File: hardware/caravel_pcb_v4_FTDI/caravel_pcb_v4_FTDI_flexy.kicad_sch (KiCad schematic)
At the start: 65 parts, among them J1 USB_B_Micro - 10118193-0001LF, J10 Conn_01x27_Female, J11 Conn_01x20_Female, J2 Conn_01x02_Female, J3 Conn_01x02_Male, J4 Conn_01x04_Female, J5 Conn_01x02_Male, J6 Conn_01x02_Male, J7 Conn_01x06_Female, J8 Conn_01x02_Male, J9 Conn_01x02_Male, SW1 SW_Push - SKQGADE010, T1 Logo, T2 Logo, U1 FT232H, U2 SN74LVC1G125DCKR, U3 SN74LVC1G125DCKR, U4 AZ1117CH-1.8TRG1, U5 AZ1117-3.3, U6 caravel_breakout, U7 W25Q32FVSS, X1 DSC6001_10MHZ, Y1 CSTNE12M0GH5L000R0

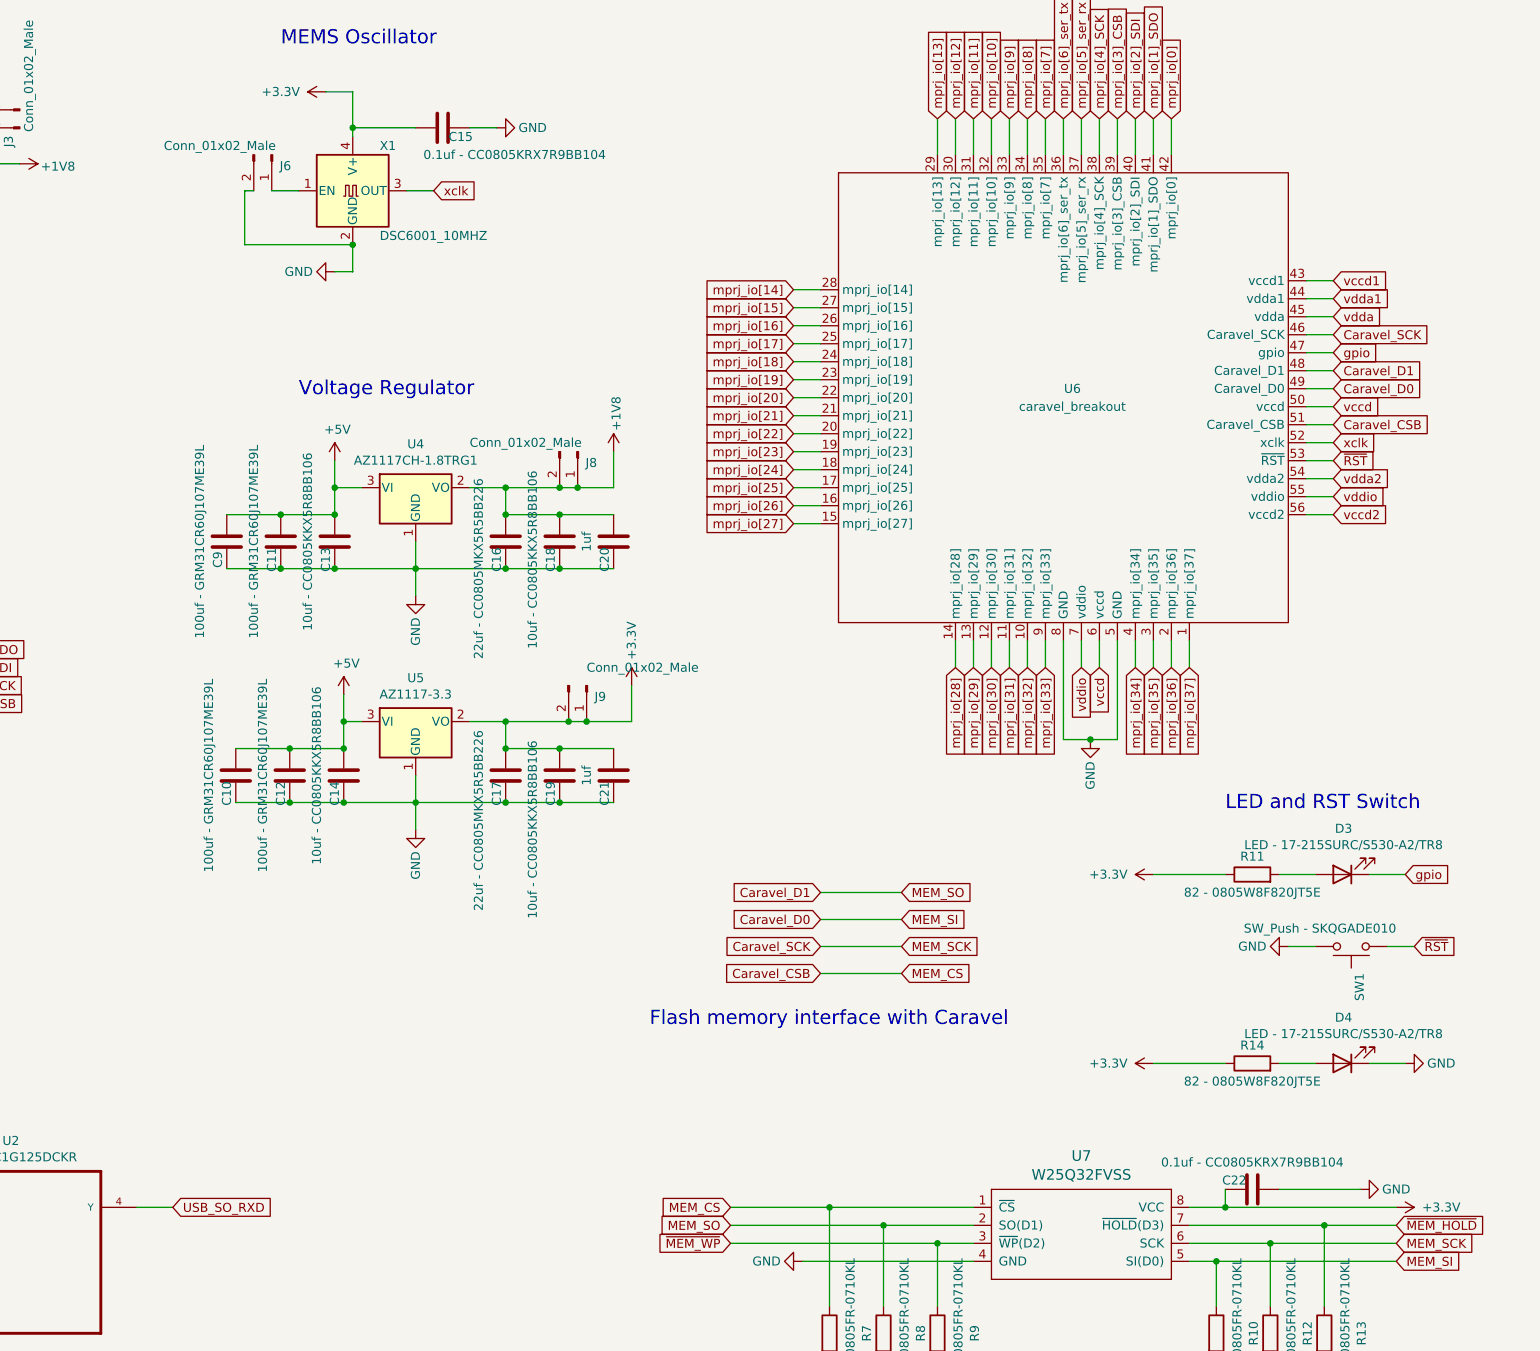
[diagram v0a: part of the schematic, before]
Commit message: update caravel FTDI mainboard V4 (Rev 4B)
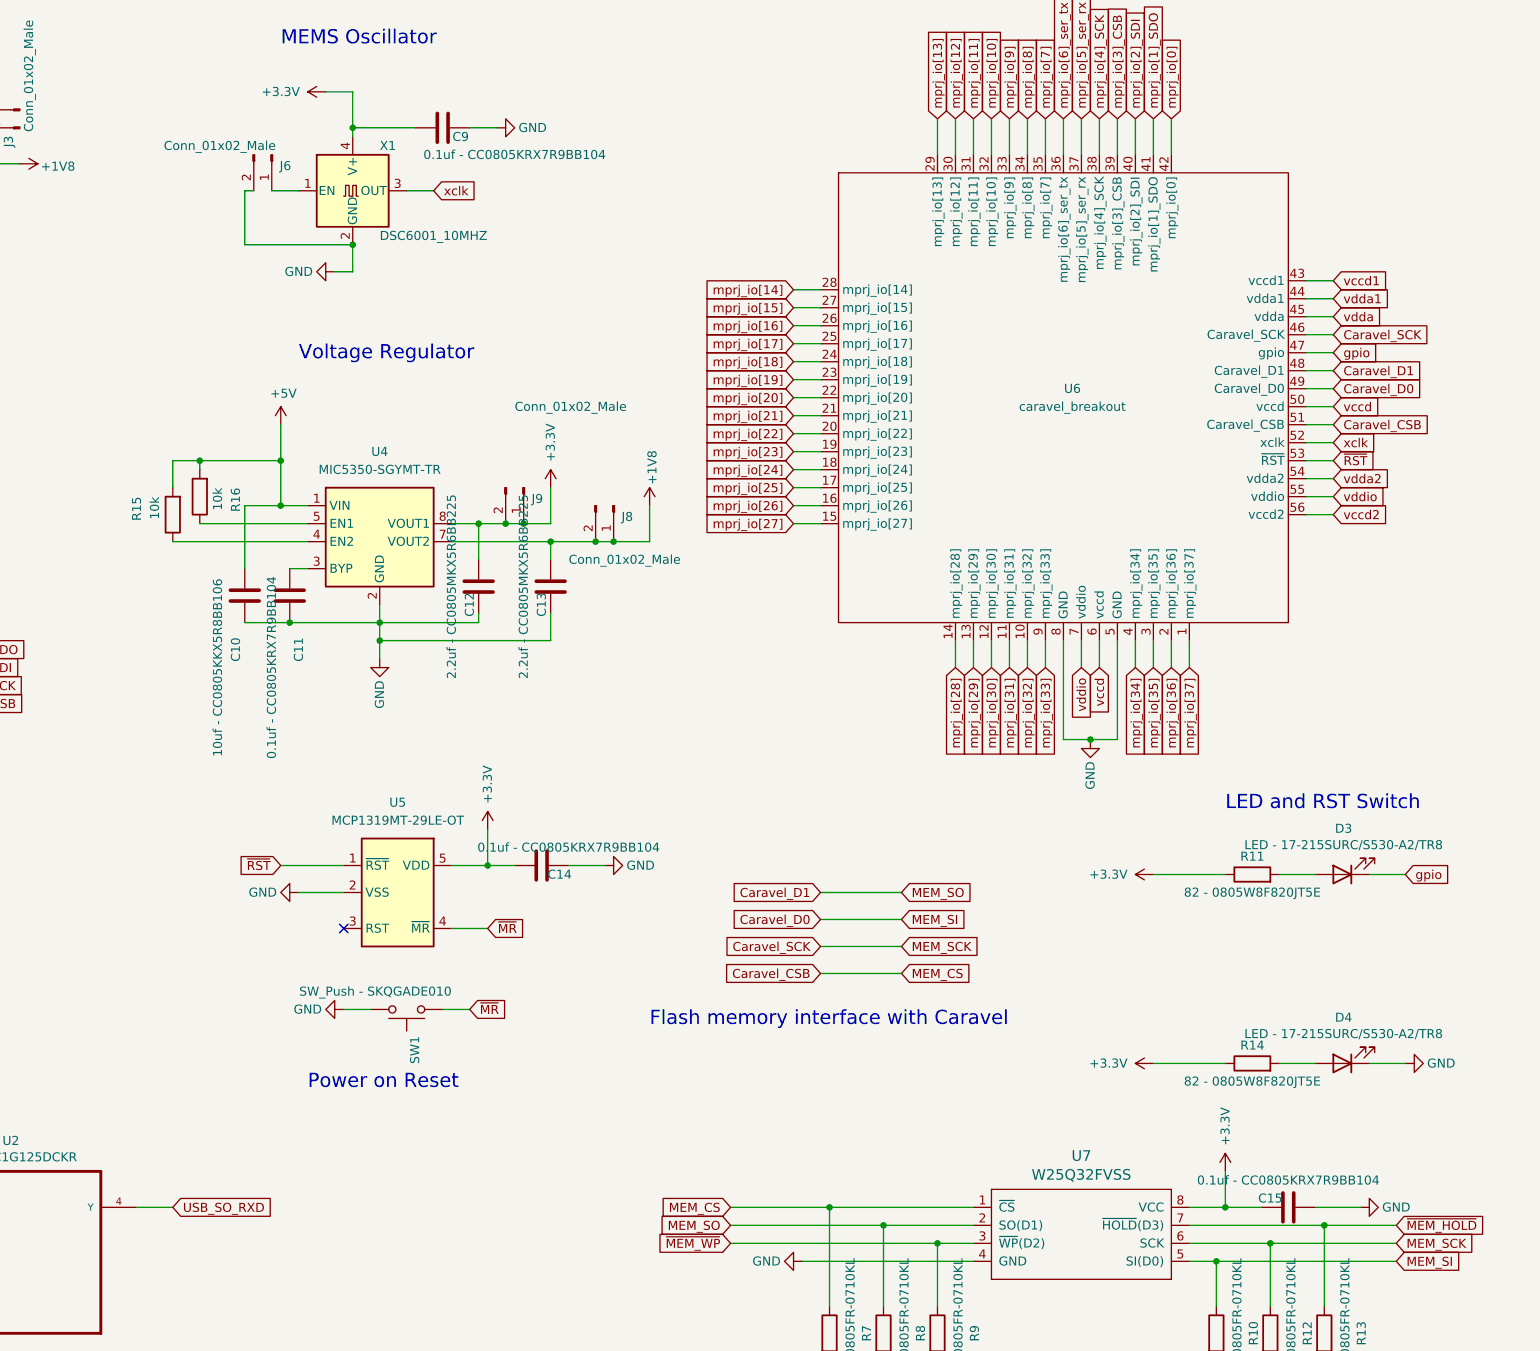
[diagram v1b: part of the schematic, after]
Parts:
- removed C16, C17: 22uf - CC0805MKX5R5BB226, Capacitor_SMD:C_0805_2012Metric, symbol Device:C
- removed C18, C19: 10uf - CC0805KKX5R8BB106, Capacitor_SMD:C_0805_2012Metric, symbol Device:C
- removed C20, C21: 1uf, Capacitor_SMD:C_0805_2012Metric, symbol Device:C
- removed C9: 100uf - GRM31CR60J107ME39L, Capacitor_SMD:C_1206_3216Metric, symbol Device:C
- removed U4: AZ1117CH-1.8TRG1, Package_TO_SOT_SMD:SOT-223, symbol Regulator_Linear:AZ1117-1.8
- removed U5: AZ1117-3.3, Package_TO_SOT_SMD:SOT-223, symbol Regulator_Linear:AZ1117-3.3
- added R15, R16: 10k, Resistor_SMD:R_0805_2012Metric, symbol Device:R
- added U4: MIC5350-SGYMT-TR, Package_DFN_QFN:DFN-8-1EP_2x2mm_P0.5mm_EP0.6x1.2mm, symbol Caravel_board:MIC5350-SGYMT-TR
- added U5: MCP1319MT-29LE-OT, Caravel_Board:PoR_5_SOT23, symbol Caravel_board:MCP1319MT-29LE-OT
- C10: value 100uf - GRM31CR60J107ME39L -> 10uf - CC0805KKX5R8BB106; footprint Capacitor_SMD:C_1206_3216Metric -> Capacitor_SMD:C_0805_2012Metric
- C11: value 100uf - GRM31CR60J107ME39L -> 0.1uf - CC0805KRX7R9BB104; footprint Capacitor_SMD:C_1206_3216Metric -> Capacitor_SMD:C_0805_2012Metric
- C12: value 100uf - GRM31CR60J107ME39L -> 2.2uf - CC0805MKX5R6BB225; footprint Capacitor_SMD:C_1206_3216Metric -> Capacitor_SMD:C_0805_2012Metric
- C13: value 10uf - CC0805KKX5R8BB106 -> 2.2uf - CC0805MKX5R6BB225
- C14: value 10uf - CC0805KKX5R8BB106 -> 0.1uf - CC0805KRX7R9BB104
- renumbered C22 to C15, C15 to C9
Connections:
- net +1V8: now also C13.2, U4.7 (VOUT2)
- net +3V3: now also C12.2, C14.2, U4.8 (VOUT1), U5.5 (VDD)
- net +5V: now also R15.2, R16.2, U4.1 (VIN); no longer C11.2, C12.2, C13.2, C14.2
- net GND: now also C11.2, U4.2 (GND), U4.9 (GND), U5.2 (VSS); no longer C11.1
- net ~{RST}: now also U5.1 (~{RST}); no longer SW1.1
- new net: R16.1, U4.5 (EN1)
- new net: R15.1, U4.4 (EN2)
- new net: C11.1, U4.3 (BYP)
- new net ~{MR}: SW1.1, U5.4 (~{MR})
- no-connect marks 16 -> 17
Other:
- note added: "Power on Reset"
- moved on the sheet: C15, J8, J9, SW1

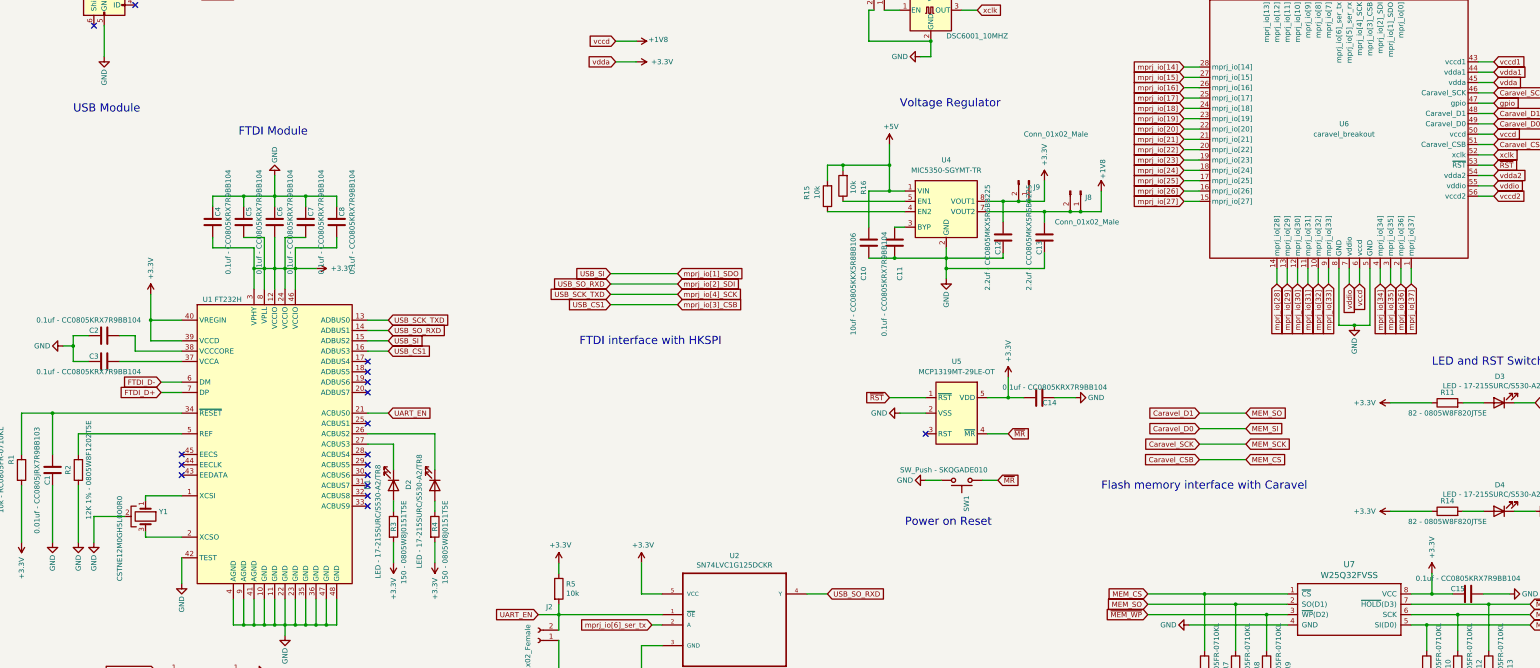
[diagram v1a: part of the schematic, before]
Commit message: update caravel FTDI mainboard V4 (Rev 4B) to support different LDO devices with the same footprint
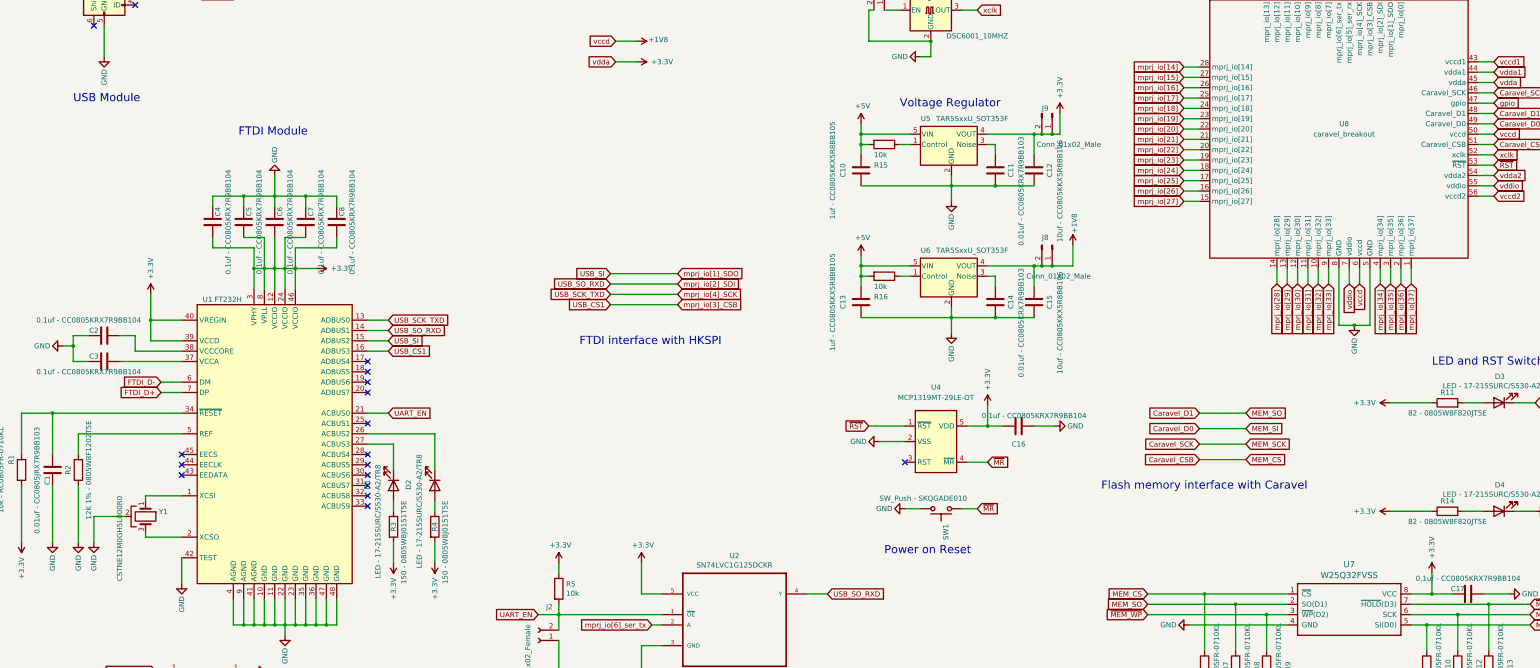
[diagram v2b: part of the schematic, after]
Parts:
- removed U4: MIC5350-SGYMT-TR, Package_DFN_QFN:DFN-8-1EP_2x2mm_P0.5mm_EP0.6x1.2mm, symbol Caravel_board:MIC5350-SGYMT-TR
- added C14: 0.01uf - CC0805KRX7R9BB103, Capacitor_SMD:C_0805_2012Metric, symbol Device:C
- added C15: 10uf - CC0805KKX5R8BB106, Capacitor_SMD:C_0805_2012Metric, symbol Device:C
- added U5, U6: TAR5SxxU_SOT353F, Caravel_Board:SOT-353F, symbol Caravel_board:TAR5SxxU_SOT353F
- C10: value 10uf - CC0805KKX5R8BB106 -> 1uf - CC0805KKX5R8BB105
- C11: value 0.1uf - CC0805KRX7R9BB104 -> 0.01uf - CC0805KRX7R9BB103
- C12: value 2.2uf - CC0805MKX5R6BB225 -> 10uf - CC0805KKX5R8BB106
- C13: value 2.2uf - CC0805MKX5R6BB225 -> 1uf - CC0805KKX5R8BB105
- renumbered C14 to C16, C15 to C17, U5 to U4, U6 to U8
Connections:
- net +1V8: now also C15.2, U6.4 (VOUT); no longer C13.2
- net +3V3: now also U5.4 (VOUT)
- net +5V: now also C13.2, U5.5 (VIN), U6.5 (VIN)
- net GND: now also C14.2, C15.1, U5.2 (GND), U6.2 (GND)
- net at R16.1: now also U6.1 (Control)
- net at R15.1: now also U5.1 (Control)
- net at C11.1: now also U5.3 (Noise)
- new net: C14.1, U6.3 (Noise)
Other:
- moved on the sheet: C10, C11, C16, J8, J9, R15, SW1, U4
